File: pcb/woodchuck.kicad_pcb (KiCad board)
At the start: 2 copper layers, 58 x 35 mm, 40 parts, among them IC1 24AA01, IC101 ADP3335, IC201 u-blox_CAM-M8Q, IC601 MS5611-01BA03, J401 JSTA-4, P101 CONN_01X02, P401 SWD, P402 USB_OTG, SW401 SPST, U301 Radiometrix_MTX2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

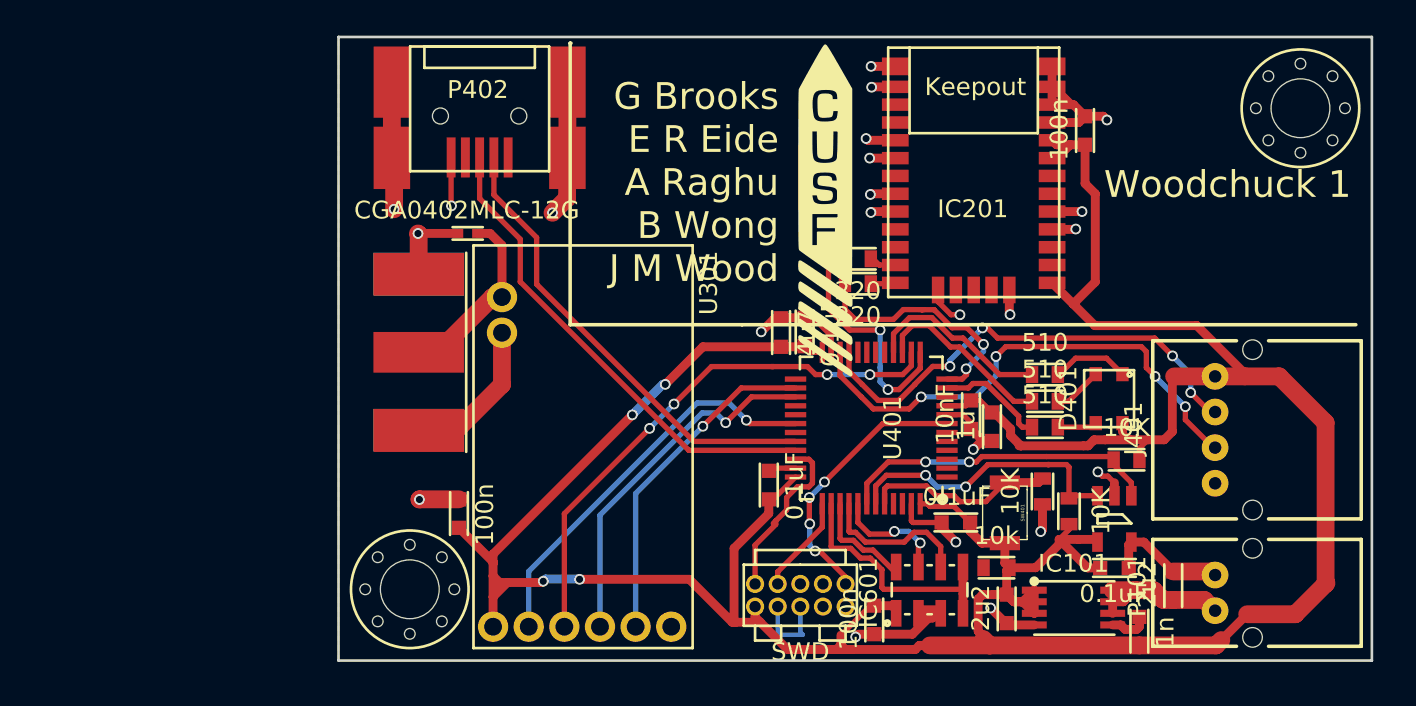
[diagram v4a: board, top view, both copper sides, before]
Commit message: Finished layout with silkscreen
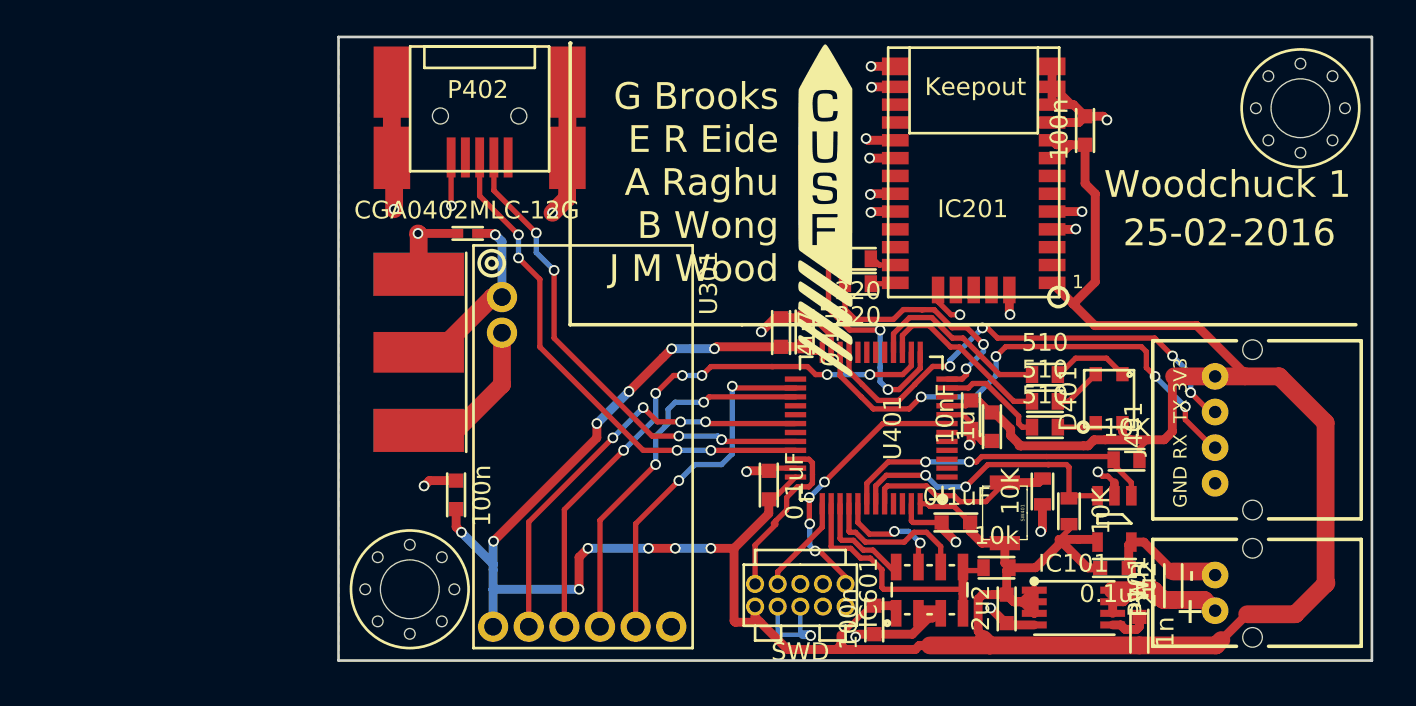
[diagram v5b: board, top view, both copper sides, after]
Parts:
- added G***: LOGO, Woodchuck:Woodchuck_2, B.Cu at (180.3, 124.1)
- moved C301 1.06 mm to (173.6, 126.5)
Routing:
- net +3V3: track 193.8 -> 196.2 mm, vias 4 -> 11
- net /microcontroller/USB_D+: track 27.3 -> 28.8 mm, vias 0 -> 4
- net /Radio/MTX2_EN/PGM: track 22.5 -> 23.9 mm, vias 1 -> 4
- net /Radio/MTX2_P0: track 18.9 -> 20.2 mm, vias 1 -> 2
- net /barometer/BARO_CS: track 13.6 -> 14.8 mm
- net /microcontroller/USB_D-: track 26.3 -> 27.5 mm, vias 0 -> 4
- net GND: track 98.7 -> 99.9 mm, vias 23 -> 25
- net /Radio/MTX2_TXD: track 30.5 -> 31.4 mm, vias 4 -> 6
- net /Radio/MTX2_P1: track 20.4 -> 21.2 mm, vias 1 -> 2
- net Net-(A301-Pad1): track 10.5 -> 10.6 mm, vias 0 -> 1
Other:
- board text added: "+"
- board text added: "-"
- board text added: "1"
- board text added: "25-02-2016"
- board text added: "3V3"
- board text added: "GND"
- board text added: "PWR"
- board text added: "RX"
- board text added: "TX"
- board text added: "www.cusf.co.uk"

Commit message: Fix some layout issues
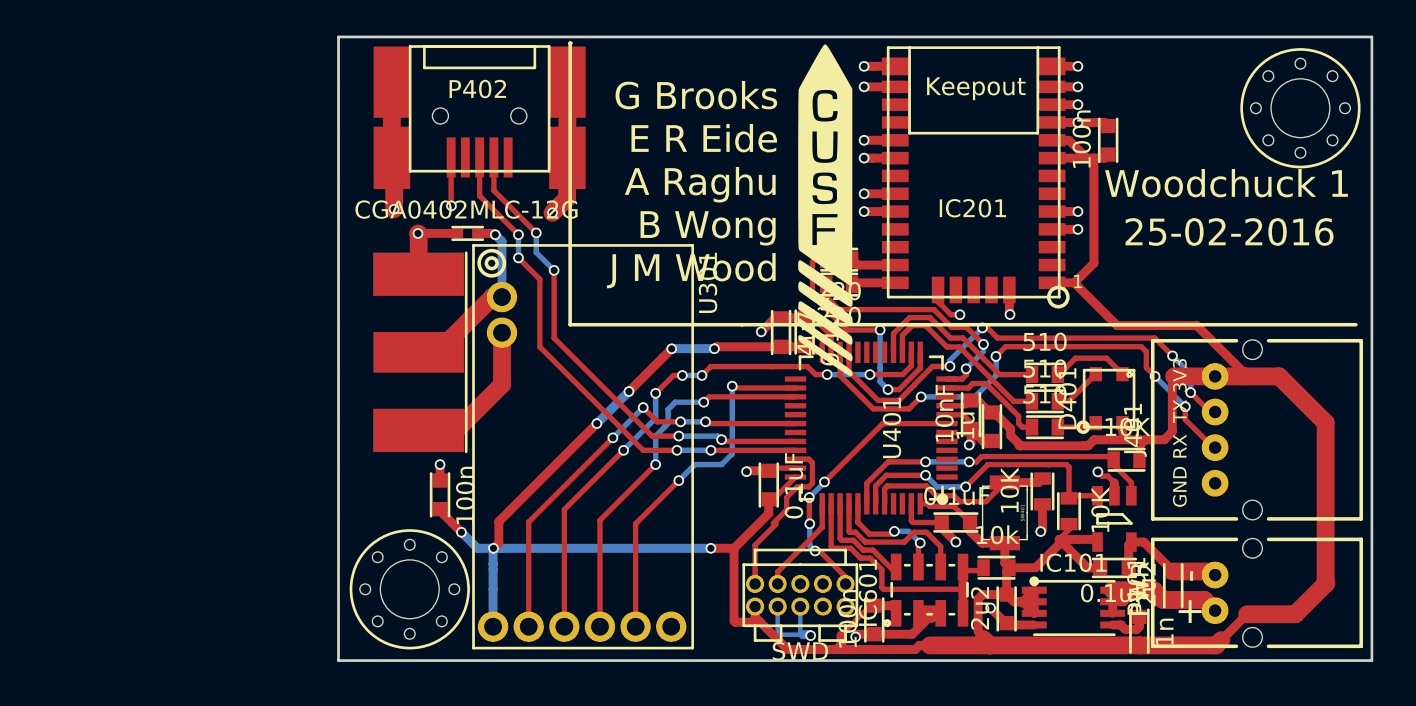
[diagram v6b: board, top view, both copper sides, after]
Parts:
- removed X404: CUSF LOGO BACK, Woodchuck:cusf_logo_full
- moved G*** 2.91 mm to (177.4, 123.9)
- moved C201 1.41 mm to (210.2, 105.0)
- moved R202 1.05 mm to (195.1, 113.9)
- moved R201 1.05 mm to (195.1, 112.5)
- moved C301 0.90 mm to (172.7, 126.5)
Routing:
- net +3V3: track 196.2 -> 194.3 mm, vias 11 -> 7
- net Net-(IC201-Pad25): track 1.52 -> 2.67 mm
- net Net-(IC201-Pad26): track 1.40 -> 2.54 mm
- net GND: track 99.9 -> 99.3 mm, vias 25 -> 28
- added copper zone on F.Cu, net GND
- removed copper zone on F.Cu, net (none)
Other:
- net class Default: clearance 0.1 -> 0.15; via_drill 0.4 -> 0.3
- rule pad_to_mask_clearance: 0.2 -> 0
- rule trace_clearance: 0.1 -> 0.15

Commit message: Fixed vias to correct sizes, moved some components further apart from each other
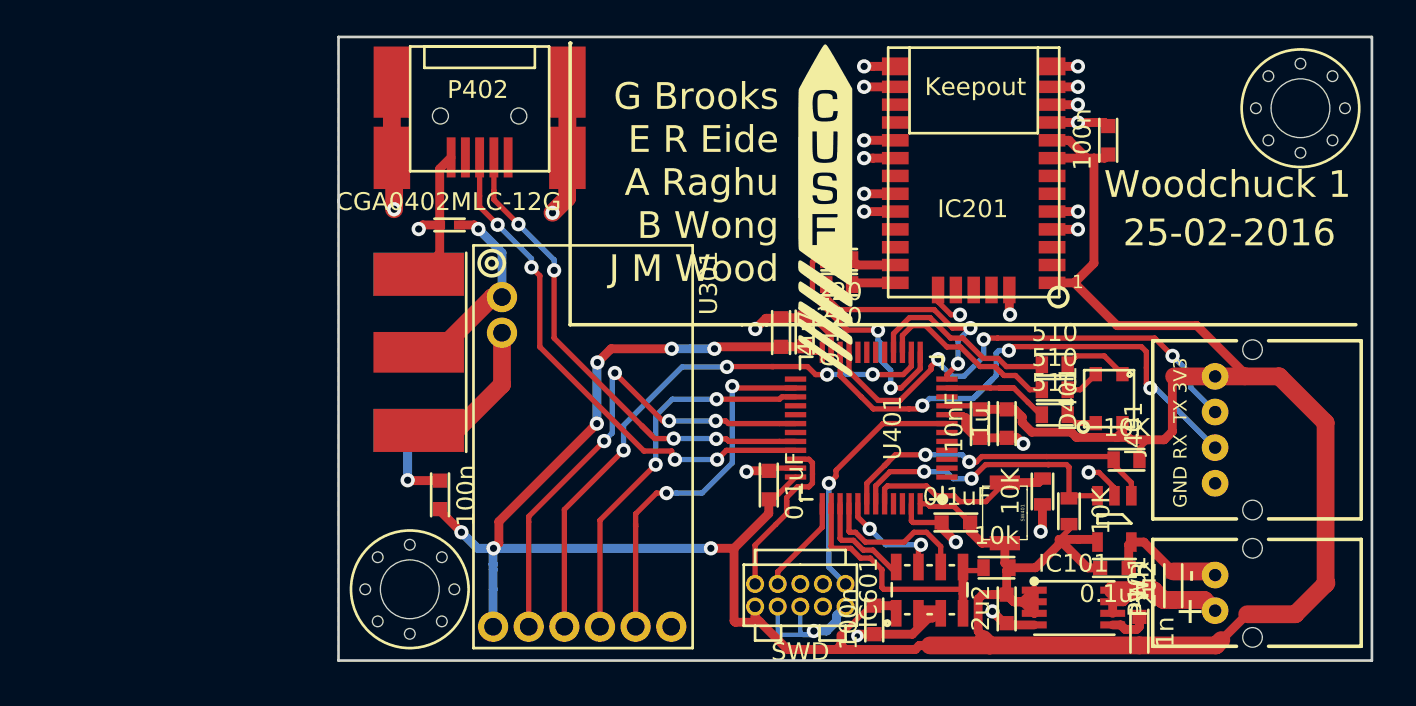
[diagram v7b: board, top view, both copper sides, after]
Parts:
- moved D301 1.13 mm to (173.8, 110.5)
- moved R401 0.89 mm to (207.2, 121.2)
- moved R402 0.85 mm to (207.2, 119.8)
- moved C405 0.84 mm to (204.5, 120.9)
- moved R403 0.78 mm to (207.2, 118.4)
- moved C401 0.71 mm to (203.0, 120.9)
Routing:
- net GND: track 99.3 -> 109.1 mm, vias 28 -> 27
- net /Radio/MTX2_EN/PGM: track 23.9 -> 27.6 mm
- net +3V3: track 194.3 -> 196.1 mm
- net /microcontroller/EXT_RX: track 28.5 -> 30.2 mm, vias 4 -> 3
- net /microcontroller/nRST: track 15.3 -> 14.2 mm, vias 4 -> 1
- net /GPS/GPS_FROM_MCU: track 13.9 -> 12.9 mm
- net /microcontroller/EXT_TX: track 26.8 -> 27.8 mm, vias 4 -> 3
- net Net-(D401-Pad1): track 2.22 -> 3.19 mm
- net Net-(A301-Pad1): track 10.6 -> 11.5 mm
- net Net-(D401-Pad4): track 2.76 -> 1.94 mm
- net /microcontroller/USB_D-: track 27.5 -> 28.3 mm
- net /Radio/MTX2_P0: track 20.2 -> 21.0 mm
- net Net-(D401-Pad3): track 4.38 -> 3.71 mm
- net Net-(IC1-Pad1): track 18.1 -> 18.8 mm
- net Net-(R401-Pad2): track 6.13 -> 6.75 mm
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
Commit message: last commit before reloading net list
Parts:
- A301: moved to B.Cu
- moved D301 2.58 mm to (173.4, 113.1), turned to 90 degrees
- moved C101 2.01 mm to (214.0, 132.0), turned to 90 degrees
- moved A301 1.80 mm to (169.7, 117.6)
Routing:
- net GND: track 109.1 -> 217.6 mm, vias 27 -> 73
- net +BATT: track 9.05 -> 4.07 mm
- net +3V3: track 196.1 -> 199.8 mm
- net Net-(A301-Pad1): track 11.5 -> 9.51 mm
